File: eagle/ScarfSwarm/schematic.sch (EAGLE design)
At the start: 5 parts

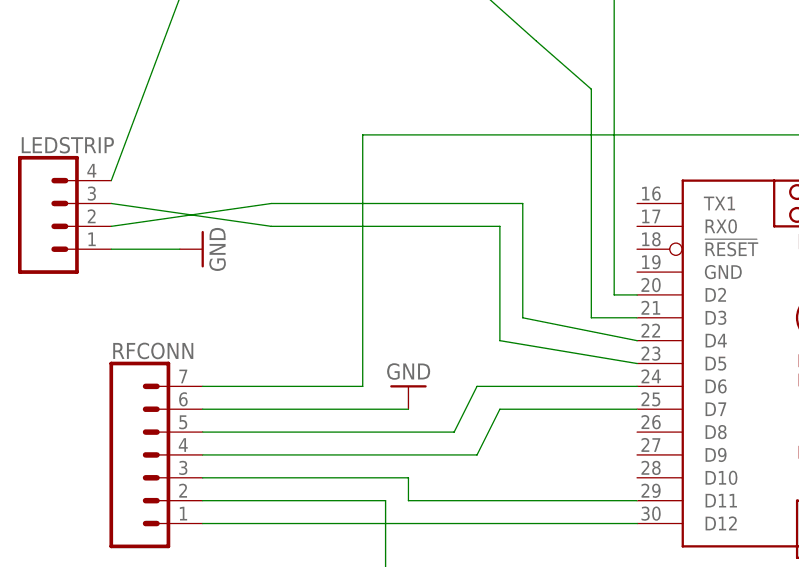
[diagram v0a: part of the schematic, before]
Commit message: rearrange JST connection for strip, bump version
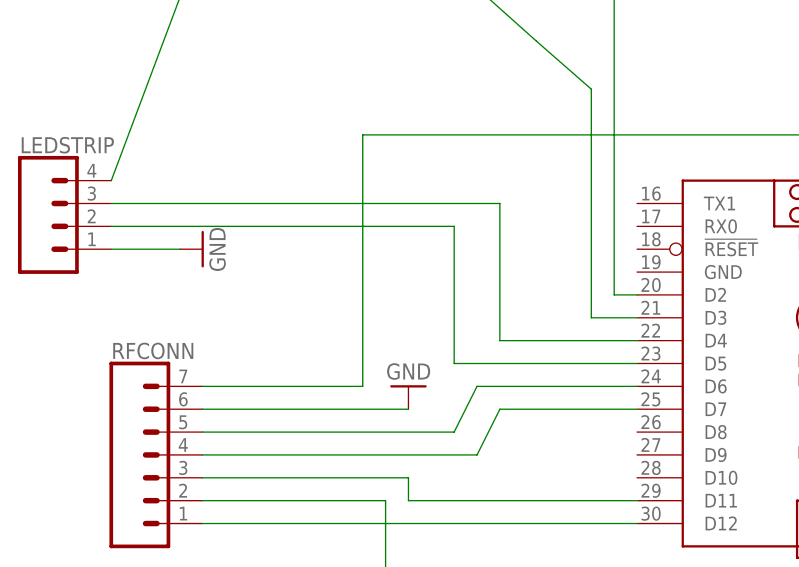
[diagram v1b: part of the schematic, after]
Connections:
- net N$13: now also SCARFYMCSCARFFACE.D4; no longer SCARFYMCSCARFFACE.D5
- net N$8: now also SCARFYMCSCARFFACE.D5; no longer SCARFYMCSCARFFACE.D4
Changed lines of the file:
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@@
 <segment>
 <pinref part="LEDSTRIP" gate="J1" pin="2"/>
-<wire x1="2.54" y1="33.02" x2="20.32" y2="35.56" width="0.1524" layer="91"/>
-<wire x1="20.32" y1="35.56" x2="48.26" y2="35.56" width="0.1524" layer="91"/>
-<wire x1="48.26" y1="35.56" x2="48.26" y2="22.86" width="0.1524" layer="91"/>
-<pinref part="SCARFYMCSCARFFACE" gate="G$1" pin="D4"/>
-<wire x1="48.26" y1="22.86" x2="60.96" y2="20.32" width="0.1524" layer="91"/>
+<wire x1="2.54" y1="33.02" x2="40.64" y2="33.02" width="0.1524" layer="91"/>
+<pinref part="SCARFYMCSCARFFACE" gate="G$1" pin="D5"/>
+<wire x1="40.64" y1="33.02" x2="40.64" y2="17.78" width="0.1524" layer="91"/>
+<wire x1="40.64" y1="17.78" x2="60.96" y2="17.78" width="0.1524" layer="91"/>
 </segment>
 </net>
@@
 <segment>
 <pinref part="LEDSTRIP" gate="J1" pin="3"/>
-<wire x1="2.54" y1="35.56" x2="20.32" y2="33.02" width="0.1524" layer="91"/>
-<wire x1="20.32" y1="33.02" x2="45.72" y2="33.02" width="0.1524" layer="91"/>
-<wire x1="45.72" y1="33.02" x2="45.72" y2="20.32" width="0.1524" layer="91"/>
-<pinref part="SCARFYMCSCARFFACE" gate="G$1" pin="D5"/>
-<wire x1="45.72" y1="20.32" x2="60.96" y2="17.78" width="0.1524" layer="91"/>
+<wire x1="2.54" y1="35.56" x2="45.72" y2="35.56" width="0.1524" layer="91"/>
+<wire x1="45.72" y1="35.56" x2="45.72" y2="20.32" width="0.1524" layer="91"/>
+<pinref part="SCARFYMCSCARFFACE" gate="G$1" pin="D4"/>
+<wire x1="45.72" y1="20.32" x2="60.96" y2="20.32" width="0.1524" layer="91"/>
 </segment>
 </net>
